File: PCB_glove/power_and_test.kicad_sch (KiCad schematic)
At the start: 21 parts, among them J9 PROTECTED +5V INPUT CONNECTOR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, U2 3V3 IMU REGULATOR / DK RAIL S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

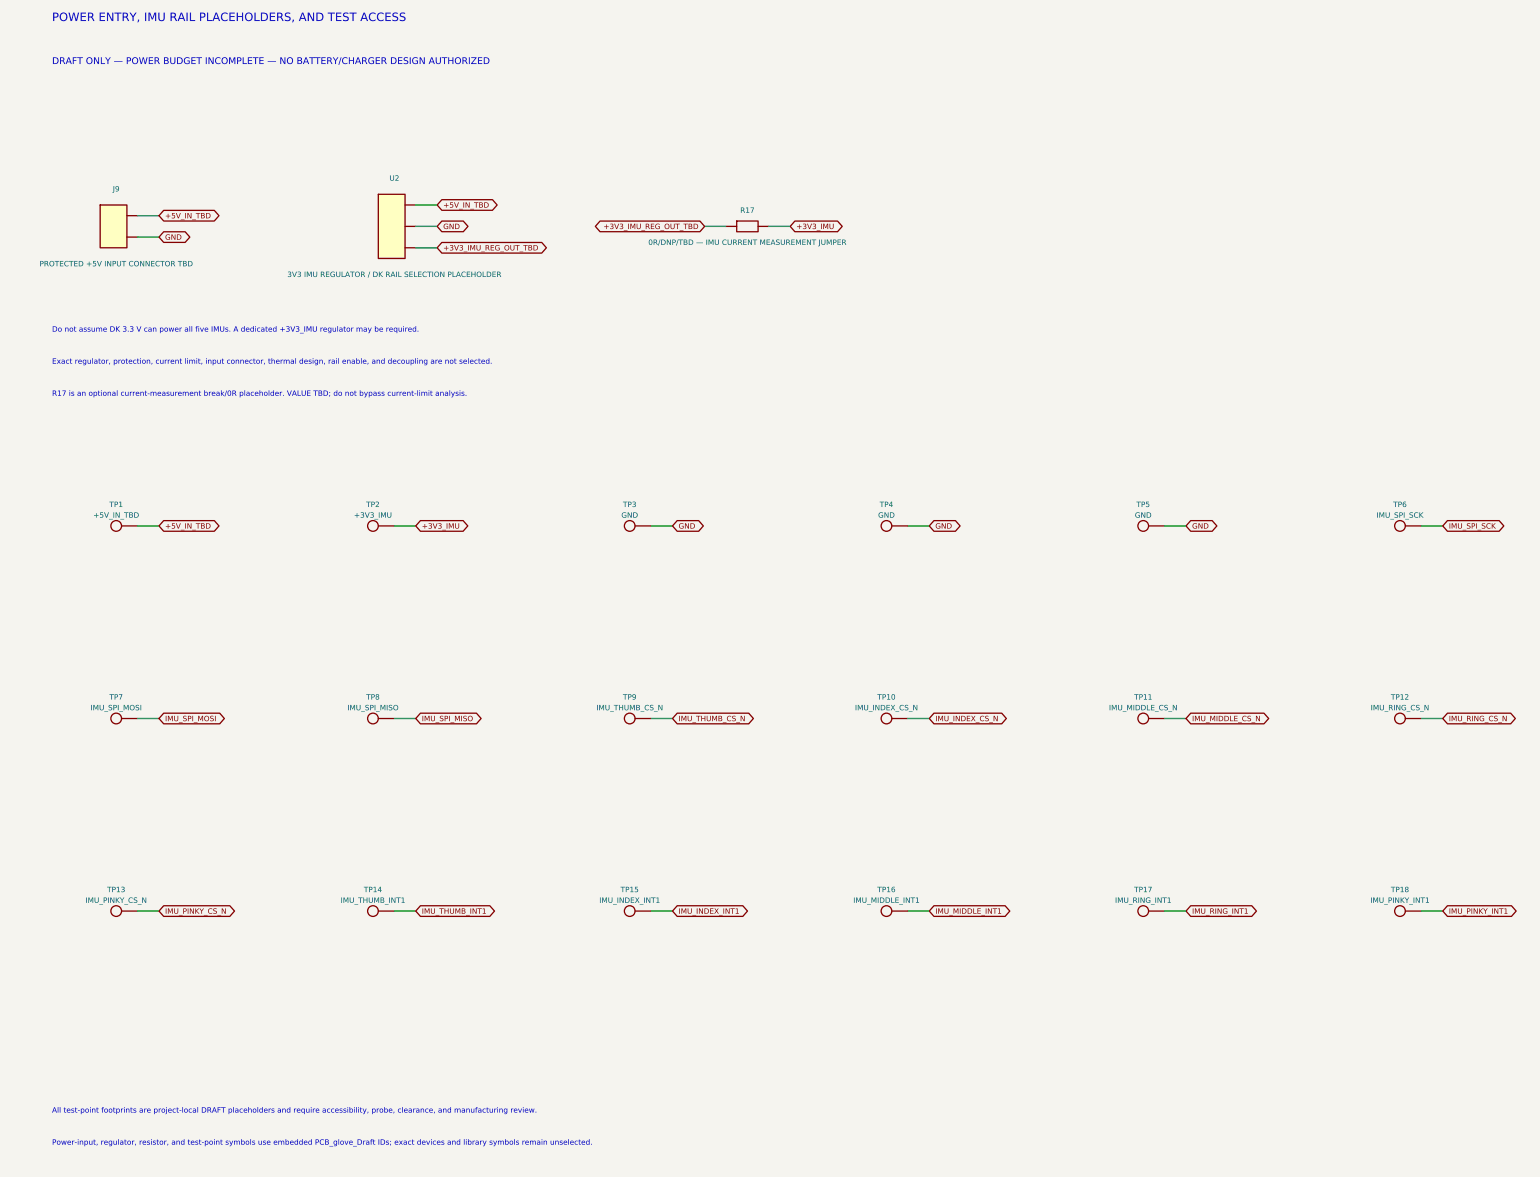
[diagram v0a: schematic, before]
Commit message: Add ERC-clean IMU power schematic update
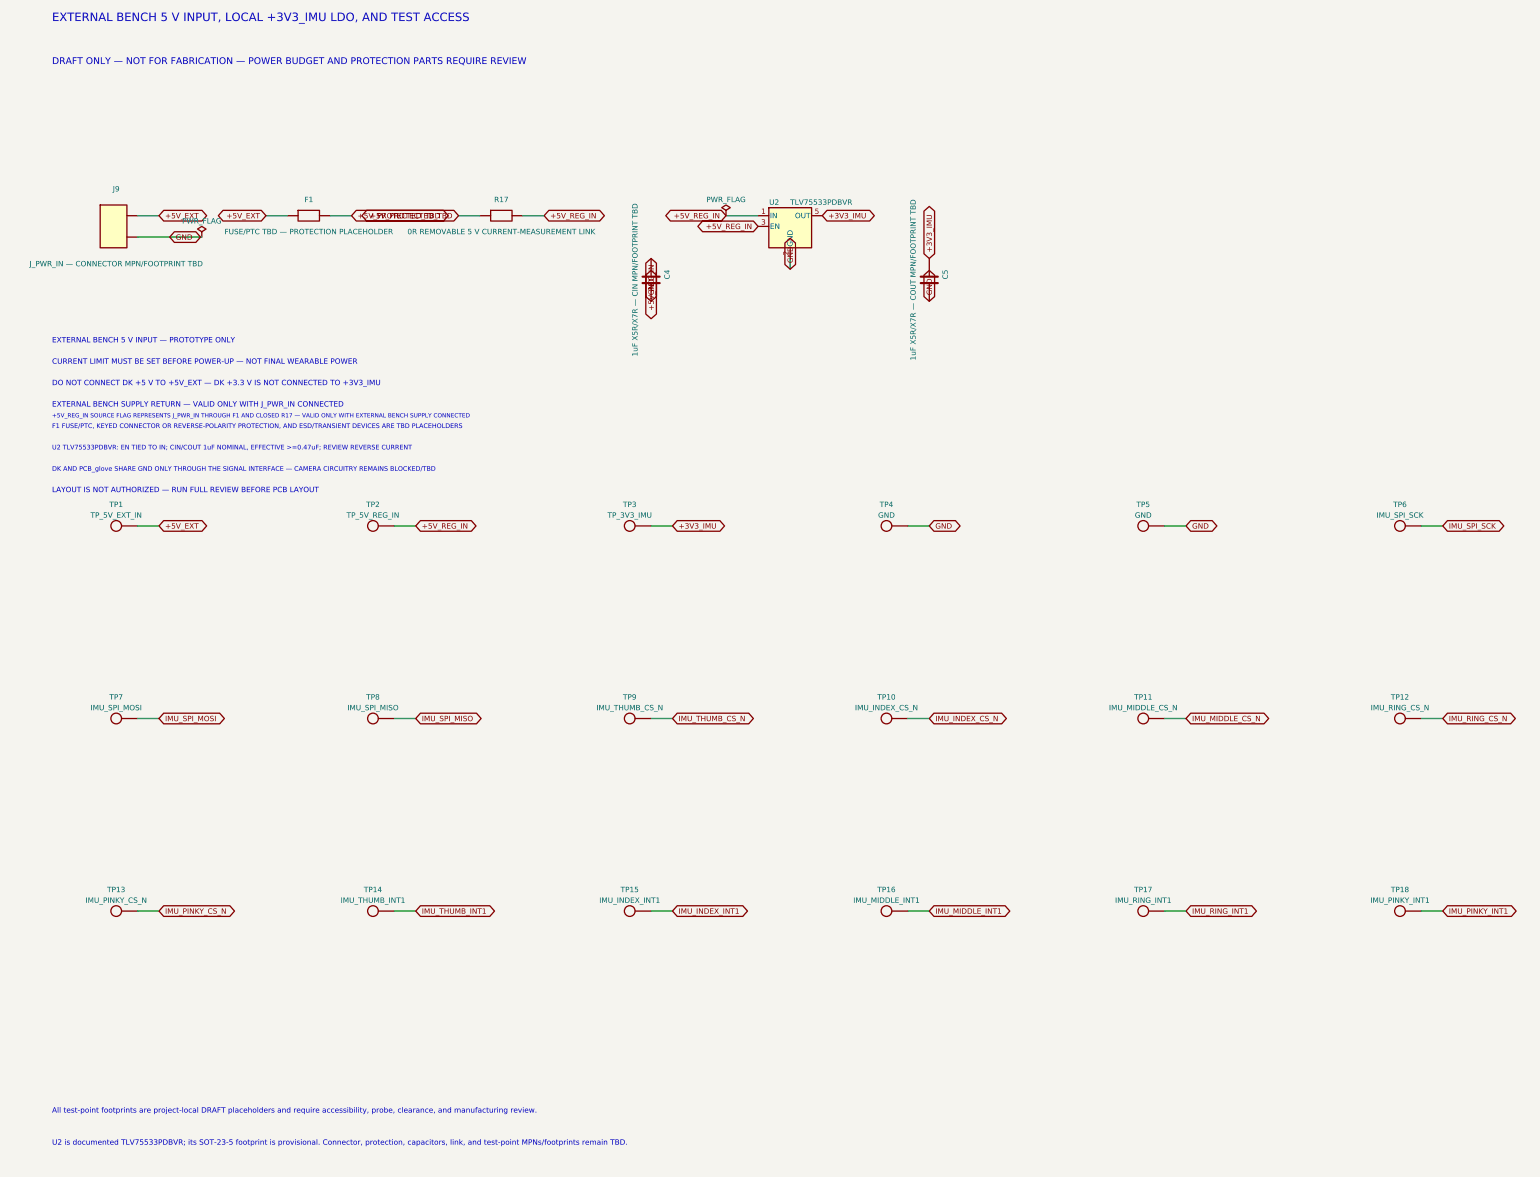
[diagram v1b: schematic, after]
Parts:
- removed U2: 3V3 IMU REGULATOR / DK RAIL SELECTION PLACEHOLDER, symbol PCB_glove_Draft:REGULATOR_PLACEHOLDER_3
- added C4: 1uF X5R/X7R — CIN MPN/FOOTPRINT TBD, symbol PCB_glove_Draft:C_OPTION
- added C5: 1uF X5R/X7R — COUT MPN/FOOTPRINT TBD, symbol PCB_glove_Draft:C_OPTION
- added F1: FUSE/PTC TBD — PROTECTION PLACEHOLDER, symbol PCB_glove_Draft:R_OPTION
- added U2: TLV75533PDBVR, Package_TO_SOT_SMD:SOT-23-5, symbol PCB_glove_Draft:TLV75533PDBV_DOCUMENTED
- J9: value PROTECTED +5V INPUT CONNECTOR TBD -> J_PWR_IN — CONNECTOR MPN/FOOTPRINT TBD
- R17: value 0R/DNP/TBD — IMU CURRENT MEASUREMENT JUMPER -> 0R REMOVABLE 5 V CURRENT-MEASUREMENT LINK
- TP1: value +5V_IN_TBD -> TP_5V_EXT_IN
- TP2: value +3V3_IMU -> TP_5V_REG_IN
- TP3: value GND -> TP_3V3_IMU
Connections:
- net +3V3_IMU: now also TP3.1, C5.2, U2.5 (OUT); no longer R17.2, TP2.1
- net GND: now also C4.1, C5.1, U2.2 (GND); no longer TP3.1
- net +3V3_IMU_REG_OUT_TBD renamed +5V_PROTECTED_TBD
- net +5V_PROTECTED_TBD: now also F1.2
- net +5V_IN_TBD renamed +5V_EXT
- net +5V_EXT: now also F1.1
- new net +5V_REG_IN: C4.2, R17.2, TP2.1, U2.1 (IN), U2.3 (EN)
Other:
- note added: "+5V_REG_IN SOURCE FLAG REPRESENTS J_PWR_IN THROUGH F1 AND CLOSED R17 — VALID ONLY WITH EXTERNAL BENCH SUPPLY CONNECTED"
- note added: "CURRENT LIMIT MUST BE SET BEFORE POWER-UP — NOT FINAL WEARABLE POWER"
- note added: "DK AND PCB_glove SHARE GND ONLY THROUGH THE SIGNAL INTERFACE — CAMERA CIRCUITRY REMAINS BLOCKED/TBD"
- note added: "DO NOT CONNECT DK +5 V TO +5V_EXT — DK +3.3 V IS NOT CONNECTED TO +3V3_IMU"
- note added: "DRAFT ONLY — NOT FOR FABRICATION — POWER BUDGET AND PROTECTION PARTS REQUIRE REVIEW"
- note added: "EXTERNAL BENCH 5 V INPUT — PROTOTYPE ONLY"
- note added: "EXTERNAL BENCH 5 V INPUT, LOCAL +3V3_IMU LDO, AND TEST ACCESS"
- note added: "EXTERNAL BENCH SUPPLY RETURN — VALID ONLY WITH J_PWR_IN CONNECTED"
- note added: "F1 FUSE/PTC, KEYED CONNECTOR OR REVERSE-POLARITY PROTECTION, AND ESD/TRANSIENT DEVICES ARE TBD PLACEHOLDERS"
- note added: "LAYOUT IS NOT AUTHORIZED — RUN FULL REVIEW BEFORE PCB LAYOUT"
- note added: "U2 TLV75533PDBVR: EN TIED TO IN; CIN/COUT 1uF NOMINAL, EFFECTIVE >=0.47uF; REVIEW REVERSE CURRENT"
- note added: "U2 is documented TLV75533PDBVR; its SOT-23-5 footprint is provisional. Connector, protection, capacitors, link, and test-point MPNs/footprints remain TBD."
- note removed: "DRAFT ONLY — POWER BUDGET INCOMPLETE — NO BATTERY/CHARGER DESIGN AUTHORIZED"
- note removed: "Do not assume DK 3.3 V can power all five IMUs. A dedicated +3V3_IMU regulator may be required."
- note removed: "Exact regulator, protection, current limit, input connector, thermal design, rail enable, and decoupling are not selected."
- note removed: "POWER ENTRY, IMU RAIL PLACEHOLDERS, AND TEST ACCESS"
- note removed: "Power-input, regulator, resistor, and test-point symbols use embedded PCB_glove_Draft IDs; exact devices and library symbols remain unselected."
- note removed: "R17 is an optional current-measurement break/0R placeholder. VALUE TBD; do not bypass current-limit analysis."
- moved on the sheet: R17

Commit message: all
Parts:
- added D1: B140-13-F — PROVISIONAL, Diode_SMD:D_SMA, symbol PCB_glove_Draft:D_SCHOTTKY_PROVISIONAL
- added TP19: TP_5V_PROTECTED, TestPoint:TestPoint_Pad_D1.5mm, symbol PCB_glove_Draft:TEST_POINT_DRAFT
- added TP20: TP_5V_FUSED, TestPoint:TestPoint_Pad_D1.5mm, symbol PCB_glove_Draft:TEST_POINT_DRAFT
- C4: value 1uF X5R/X7R — CIN MPN/FOOTPRINT TBD -> 2.2uF 10V X7R 0603 - PROVISIONAL CIN; footprint (none) -> Capacitor_SMD:C_0603_1608Metric; Characterization (none) -> https://product.tdk.com/info/en/documents/chara_sheet/C1608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; Dielectric (none) -> X7R; MPN (none) -> C1608X7R1A225K080AC; Manufacturer (none) -> TDK; Package (none) -> 0603 / 1608 metric; Status (none) -> PROVISIONAL; Voltage Rating (none) -> 10 V
- C5: value 1uF X5R/X7R — COUT MPN/FOOTPRINT TBD -> 2.2uF 10V X7R 0603 - PROVISIONAL COUT; footprint (none) -> Capacitor_SMD:C_0603_1608Metric; Characterization (none) -> https://product.tdk.com/info/en/documents/chara_sheet/C1608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; Dielectric (none) -> X7R; MPN (none) -> C1608X7R1A225K080AC; Manufacturer (none) -> TDK; Package (none) -> 0603 / 1608 metric; Status (none) -> PROVISIONAL; Voltage Rating (none) -> 10 V
- F1: value FUSE/PTC TBD — PROTECTION PLACEHOLDER -> 1206L010/30WR — PROVISIONAL; footprint (none) -> Fuse:Fuse_1206_3216Metric; Hold Current (none) -> 0.10 A at 20 C; MPN (none) -> 1206L010/30WR; Manufacturer (none) -> Littelfuse; Status (none) -> PROVISIONAL; Trip Current (none) -> 0.25 A at 20 C
- J9: value J_PWR_IN — CONNECTOR MPN/FOOTPRINT TBD -> B2B-XH-A — PROVISIONAL V1 BENCH; footprint (none) -> Connector_JST:JST_XH_B2B-XH-A_1x02_P2.50mm_Vertical; MPN (none) -> B2B-XH-A; Manufacturer (none) -> JST; Mating Housing (none) -> XHP-2; Pin Mapping (none) -> 1=+5V_EXT; 2=GND; Preferred Terminal (none) -> SXH-001T-P0.6; Status (none) -> PROVISIONAL V1 BENCH
- JP1: renamed from R17; value 0R REMOVABLE 5 V CURRENT-MEASUREMENT LINK -> TSW-102 + SNT-100 — PROVISIONAL BENCH; footprint (none) -> Connector_PinHeader_2.54mm:PinHeader_1x02_P2.54mm_Vertical; symbol PCB_glove_Draft:R_OPTION -> PCB_glove_Draft:JUMPER_HEADER_2_PROVISIONAL; Header MPN (none) -> TSW-102-07-G-S; Manufacturer (none) -> Samtec; Shunt Datasheet (none) -> https://www.samtec.com/products/snt-100-bk-g; Shunt MPN (none) -> SNT-100-BK-G; Status (none) -> PROVISIONAL BENCH ONLY
- TP1, TP2, TP3, TP4, TP5: footprint (none) -> TestPoint:TestPoint_Pad_D1.5mm
- U2: MPN (none) -> TLV75533PDBVR; Manufacturer (none) -> Texas Instruments; Package (none) -> DBV / SOT-23-5; Status (none) -> PROVISIONAL FOOTPRINT
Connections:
- net +5V_PROTECTED_TBD renamed +5V_FUSED
- net +5V_FUSED: now also D1.2 (A), TP20.1; no longer JP1.1
- new net +5V_PROTECTED: D1.1 (K), JP1.1, TP19.1
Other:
- note added: "+5V_REG_IN SOURCE FLAG REPRESENTS J_PWR_IN THROUGH F1, D1, AND CLOSED JP1 — VALID ONLY WITH EXTERNAL BENCH SUPPLY CONNECTED"
- note added: "ESD PLACEHOLDER HAS NO SELECTED MPN OR POPULATED FOOTPRINT — DO NOT ADD AN UNVERIFIED TVS"
- note added: "F1 1206L010/30WR AND D1 B140-13-F ARE PROVISIONAL; INPUT ESD REMAINS DNP/TBD"
- note added: "J9/F1/D1/JP1/U2/C4/C5 fields and footprints are provisional selections only; no production land-pattern or wearable-mechanical verification is claimed."
- note added: "JP1 IS A BENCH-ONLY REMOVABLE CURRENT SHUNT; TALL/SNAG-PRONE AND NOT A FINAL WEARABLE CHOICE"
- note added: "JST XH IS BENCH-PROTOTYPE ONLY; TALL/SNAG-PRONE FOR FINAL WEARABLE"
- note added: "PIN 1 = +5V_EXT — PIN 2 = GND"
- note added: "POWER ORDER: J9 -> F1 -> +5V_FUSED / TP20 -> D1 -> +5V_PROTECTED / TP19 -> JP1 -> U2"
- note added: "PPTC IS SECONDARY PROTECTION — BENCH-SUPPLY CURRENT LIMIT IS PRIMARY DURING BRING-UP"
- note added: "Power test-point pads, including TP20 / TP_5V_FUSED on the F1-D1 node, use provisional 1.5 mm KiCad footprints; accessibility, spacing, finish, and probe-slip risk require layout review."
- note added: "U2 DBV FOOTPRINT OVERLAY AND PIN-1 ORIENTATION ARE REQUIRED BEFORE LAYOUT; REVERSE-CURRENT/BACKFEED BEHAVIOR REMAINS OPEN."
- note added: "U2 TLV75533PDBVR: EN TIED TO IN; CIN/COUT 2.2uF NOMINAL, EFFECTIVE >0.47uF; REVIEW REVERSE CURRENT"
- note added: "VERIFY CABLE POLARITY: XHP-2 CAVITY 1 = +5 V, CAVITY 2 = GND"
- note added: "VERIFY D1 CATHODE BAND ORIENTATION BEFORE LAYOUT — K/PAD 1 FACES +5V_PROTECTED"
- note removed: "+5V_REG_IN SOURCE FLAG REPRESENTS J_PWR_IN THROUGH F1 AND CLOSED R17 — VALID ONLY WITH EXTERNAL BENCH SUPPLY CONNECTED"
- note removed: "All test-point footprints are project-local DRAFT placeholders and require accessibility, probe, clearance, and manufacturing review."
- note removed: "F1 FUSE/PTC, KEYED CONNECTOR OR REVERSE-POLARITY PROTECTION, AND ESD/TRANSIENT DEVICES ARE TBD PLACEHOLDERS"
- note removed: "U2 TLV75533PDBVR: EN TIED TO IN; CIN/COUT 1uF NOMINAL, EFFECTIVE >=0.47uF; REVIEW REVERSE CURRENT"
- note removed: "U2 is documented TLV75533PDBVR; its SOT-23-5 footprint is provisional. Connector, protection, capacitors, link, and test-point MPNs/footprints remain TBD."
